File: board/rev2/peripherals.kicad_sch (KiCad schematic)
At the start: 8 parts, among them J3 USB_C_Receptacle_USB2.0_14P, J6 Micro_SD_Card_Det1, J7 Conn_01x09_Pin, SW1 SW_Push

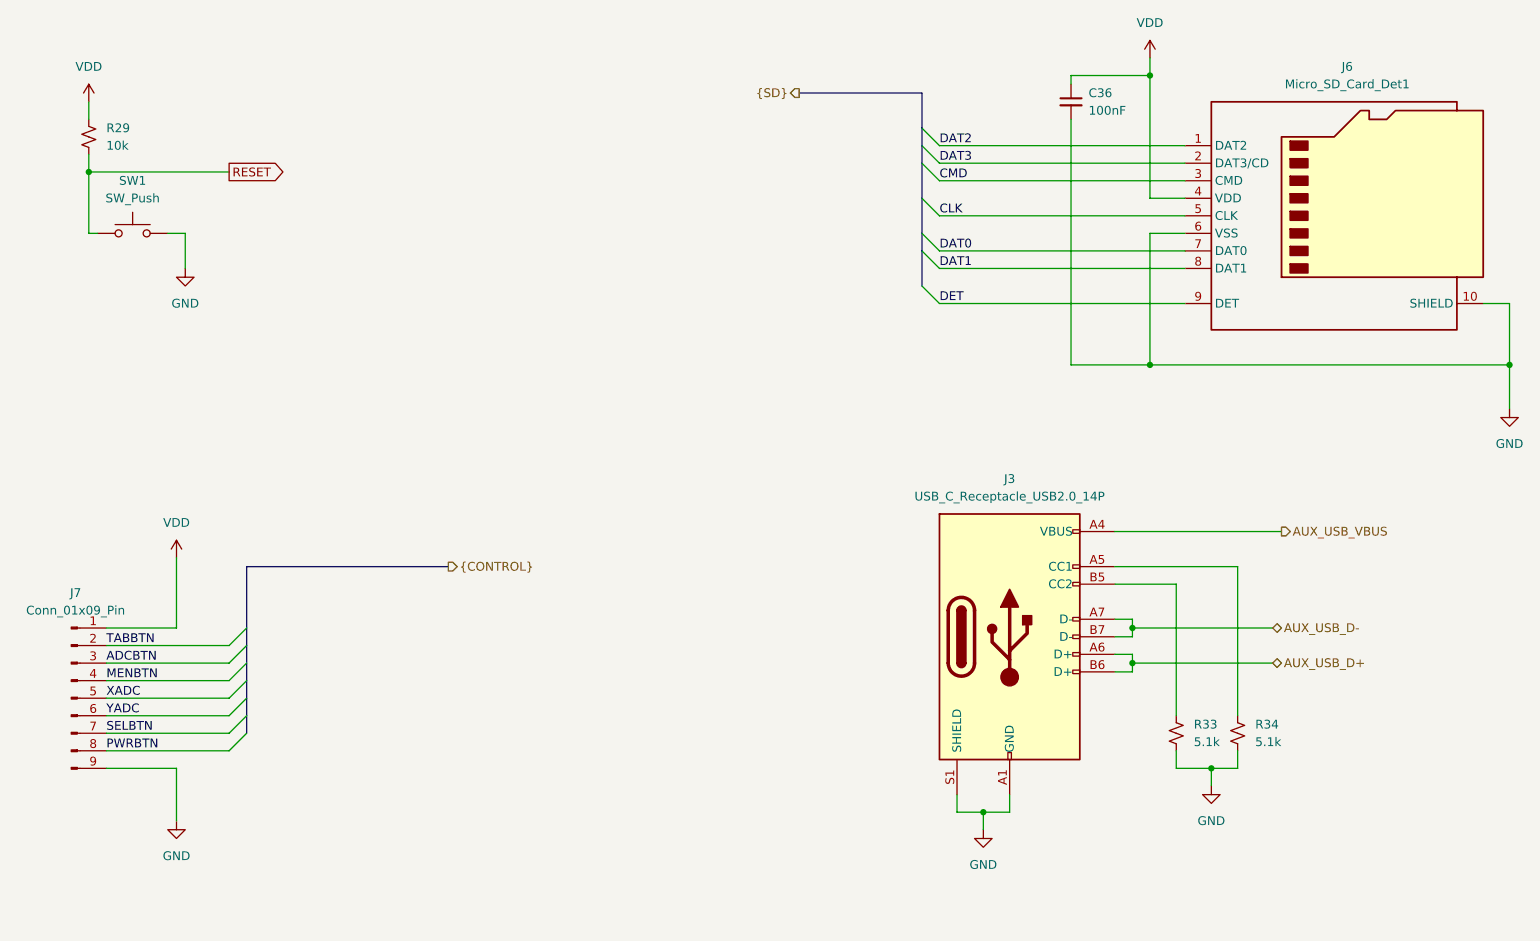
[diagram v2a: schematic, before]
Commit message: Start new PCB
- all footprints setup
- need to setup netclasses next, tho
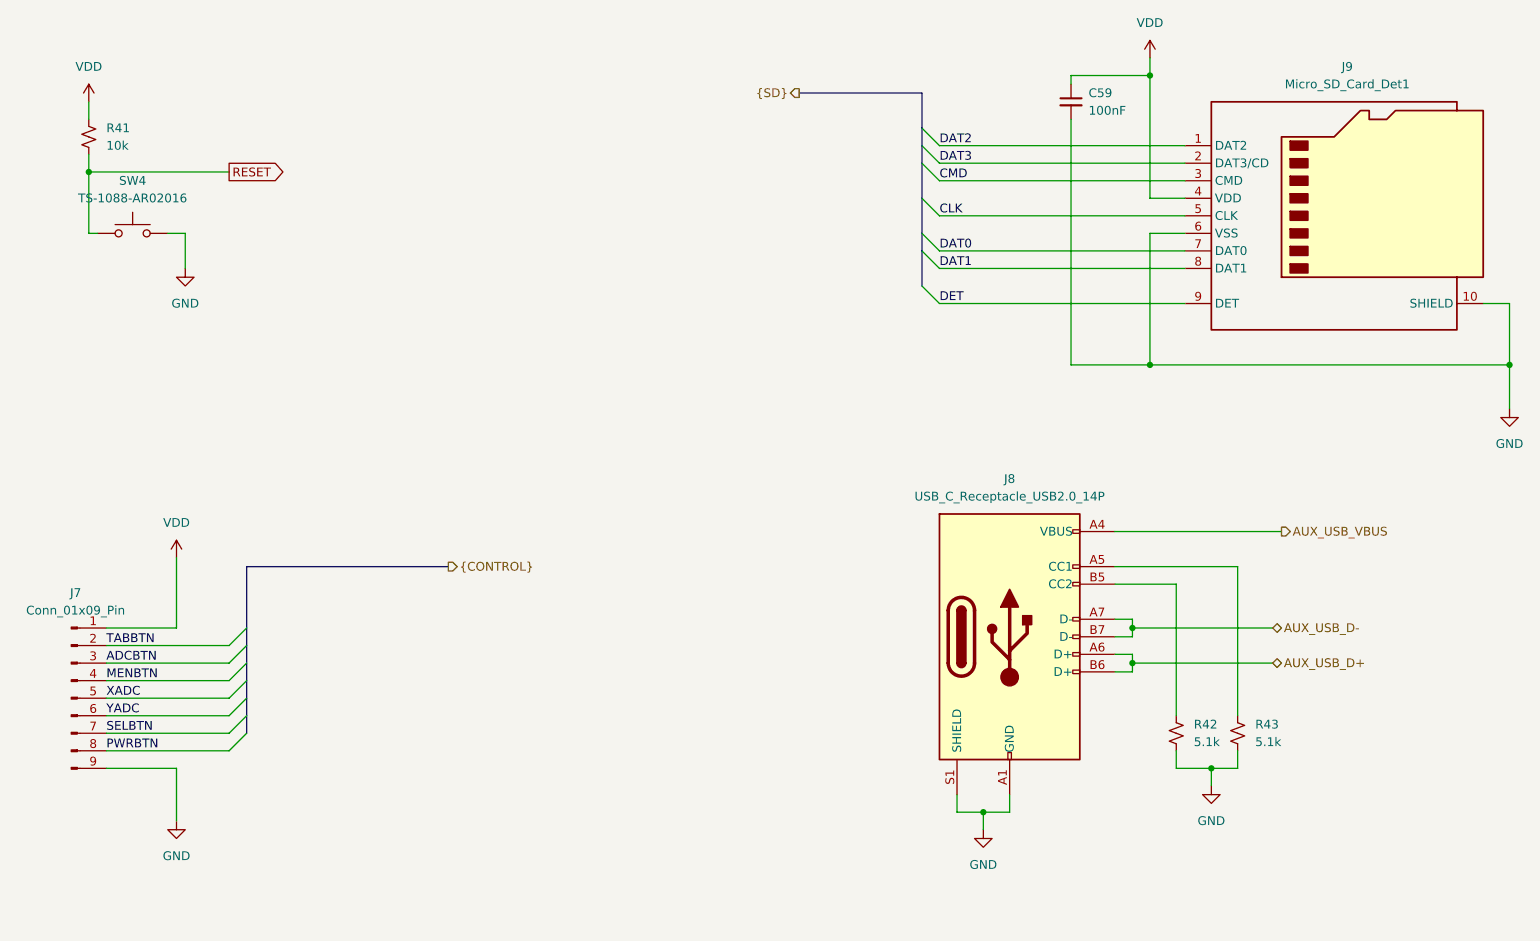
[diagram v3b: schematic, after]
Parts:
- J8: renamed from J3; footprint (none) -> Connector_USB:USB_C_Receptacle_HRO_TYPE-C-31-M-12; Part (none) -> TYPE-C-31-M-12
- J9: renamed from J6; Part (none) -> DM3AT-SF-PEJM5
- SW4: renamed from SW1; value SW_Push -> TS-1088-AR02016; footprint (none) -> Button_Switch_SMD:SW_SPST_TS-1088-xR020; Part (none) -> TS-1088-AR02016
- renumbered C36 to C59, R29 to R41, R33 to R42, R34 to R43
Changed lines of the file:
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@@
 		(dnp no)
 		(fields_autoplaced yes)
-		(property "Reference" "SW1"
+		(property "Reference" "SW4"
 			(at 57.15 54.61 0)
 			(effects
@@
 			)
 		)
-		(property "Value" "SW_Push"
+		(property "Value" "TS-1088-AR02016"
 			(at 57.15 57.15 0)
 			(effects
@@
 			)
 		)
-		(property "Footprint" ""
+		(property "Footprint" "Button_Switch_SMD:SW_SPST_TS-1088-xR020"
 			(at 57.15 57.15 0)
 			(effects
@@
 			)
 		)
+		(property "Part" "TS-1088-AR02016"
+			(at 57.15 62.23 0)
+			(effects
+				(font
+					(size 1.27 1.27)
+				)
+				(hide yes)
+			)
+		)
 		(pin "1"
 		)
@@
 			(project ""
 				(path "/32eb05c7-b4a6-42f3-8fb3-43453631100f/802ce1c9-2668-4fe7-971c-9ba57eb1ffa9"
-					(reference "SW1")
+					(reference "SW4")
 					(unit 1)
 				)
@@
 		(dnp no)
 		(fields_autoplaced yes)
-		(property "Reference" "#PWR038"
+		(property "Reference" "#PWR054"
 			(at 204.47 40.64 0)
 			(effects
@@
 			(project ""
 				(path "/32eb05c7-b4a6-42f3-8fb3-43453631100f/802ce1c9-2668-4fe7-971c-9ba57eb1ffa9"
-					(reference "#PWR038")
+					(reference "#PWR054")
 					(unit 1)
 				)
@@
 		(dnp no)
 		(fields_autoplaced yes)
-		(property "Reference" "J6"
+		(property "Reference" "J9"
 			(at 233.045 38.1 0)
 			(effects
@@
 			)
 		)
+		(property "Part" "DM3AT-SF-PEJM5"
+			(at 232.41 59.69 0)
+			(effects
+				(font
+					(size 1.27 1.27)
+				)
+				(hide yes)
+			)
+		)
 		(pin "1"
 		)
@@
 			(project ""
 				(path "/32eb05c7-b4a6-42f3-8fb3-43453631100f/802ce1c9-2668-4fe7-971c-9ba57eb1ffa9"
-					(reference "J6")
+					(reference "J9")
 					(unit 1)
 				)
@@
 		(dnp no)
 		(fields_autoplaced yes)
-		(property "Reference" "#PWR014"
+		(property "Reference" "#PWR055"
 			(at 213.36 148.59 0)
 			(effects
@@
 			(project ""
 				(path "/32eb05c7-b4a6-42f3-8fb3-43453631100f/802ce1c9-2668-4fe7-971c-9ba57eb1ffa9"
-					(reference "#PWR014")
+					(reference "#PWR055")
 					(unit 1)
 				)
@@
 		(dnp no)
 		(fields_autoplaced yes)
-		(property "Reference" "J3"
+		(property "Reference" "J8"
 			(at 184.15 97.79 0)
 			(effects
@@
 			)
 		)
-		(property "Footprint" ""
+		(property "Footprint" "Connector_USB:USB_C_Receptacle_HRO_TYPE-C-31-M-12"
 			(at 187.96 120.65 0)
 			(effects
@@
 			)
 		)
+		(property "Part" "TYPE-C-31-M-12"
+			(at 184.15 120.65 0)
+			(effects
+				(font
+					(size 1.27 1.27)
+				)
+				(hide yes)
+			)
+		)
 		(pin "B6"
 		)
@@
 			(project "mainboard"
 				(path "/32eb05c7-b4a6-42f3-8fb3-43453631100f/802ce1c9-2668-4fe7-971c-9ba57eb1ffa9"
-					(reference "J3")
+					(reference "J8")
 					(unit 1)
 				)
@@
 		(dnp no)
 		(fields_autoplaced yes)
-		(property "Reference" "#PWR013"
+		(property "Reference" "#PWR053"
 			(at 180.34 154.94 0)
 			(effects
@@
 			(project "mainboard"
 				(path "/32eb05c7-b4a6-42f3-8fb3-43453631100f/802ce1c9-2668-4fe7-971c-9ba57eb1ffa9"
-					(reference "#PWR013")
+					(reference "#PWR053")
 					(unit 1)
 				)
@@
 		(dnp no)
 		(fields_autoplaced yes)
-		(property "Reference" "#PWR02"
+		(property "Reference" "#PWR049"
 			(at 50.8 46.99 0)
 			(effects
@@
 			(project "mainboard"
 				(path "/32eb05c7-b4a6-42f3-8fb3-43453631100f/802ce1c9-2668-4fe7-971c-9ba57eb1ffa9"
-					(reference "#PWR02")
+					(reference "#PWR049")
 					(unit 1)
 				)
@@
 		(dnp no)
 		(fields_autoplaced yes)
-		(property "Reference" "R34"
+		(property "Reference" "R43"
 			(at 219.71 133.3499 0)
 			(effects
@@
 			(project ""
 				(path "/32eb05c7-b4a6-42f3-8fb3-43453631100f/802ce1c9-2668-4fe7-971c-9ba57eb1ffa9"
-					(reference "R34")
+					(reference "R43")
 					(unit 1)
 				)
@@
 		(dnp no)
 		(fields_autoplaced yes)
-		(property "Reference" "C36"
+		(property "Reference" "C59"
 			(at 195.58 41.9162 0)
 			(effects
@@
 			(project ""
 				(path "/32eb05c7-b4a6-42f3-8fb3-43453631100f/802ce1c9-2668-4fe7-971c-9ba57eb1ffa9"
-					(reference "C36")
+					(reference "C59")
 					(unit 1)
 				)
@@
 		(dnp no)
 		(fields_autoplaced yes)
-		(property "Reference" "#PWR039"
+		(property "Reference" "#PWR050"
 			(at 63.5 113.03 0)
 			(effects
@@
 			(project ""
 				(path "/32eb05c7-b4a6-42f3-8fb3-43453631100f/802ce1c9-2668-4fe7-971c-9ba57eb1ffa9"
-					(reference "#PWR039")
+					(reference "#PWR050")
 					(unit 1)
 				)
@@
 		(dnp no)
 		(fields_autoplaced yes)
-		(property "Reference" "#PWR028"
+		(property "Reference" "#PWR052"
 			(at 64.77 73.66 0)
 			(effects
@@
 			(project ""
 				(path "/32eb05c7-b4a6-42f3-8fb3-43453631100f/802ce1c9-2668-4fe7-971c-9ba57eb1ffa9"
-					(reference "#PWR028")
+					(reference "#PWR052")
 					(unit 1)
 				)
@@
 		(dnp no)
 		(fields_autoplaced yes)
-		(property "Reference" "R29"
+		(property "Reference" "R41"
 			(at 53.34 46.9899 0)
 			(effects
@@
 			(project ""
 				(path "/32eb05c7-b4a6-42f3-8fb3-43453631100f/802ce1c9-2668-4fe7-971c-9ba57eb1ffa9"
-					(reference "R29")
+					(reference "R41")
 					(unit 1)
 				)
@@
 		(dnp no)
 		(fields_autoplaced yes)
-		(property "Reference" "#PWR029"
+		(property "Reference" "#PWR056"
 			(at 256.54 93.98 0)
 			(effects
@@
 			(project ""
 				(path "/32eb05c7-b4a6-42f3-8fb3-43453631100f/802ce1c9-2668-4fe7-971c-9ba57eb1ffa9"
-					(reference "#PWR029")
+					(reference "#PWR056")
 					(unit 1)
 				)
@@
 		(dnp no)
 		(fields_autoplaced yes)
-		(property "Reference" "R33"
+		(property "Reference" "R42"
 			(at 210.82 133.3499 0)
 			(effects
@@
 			(project ""
 				(path "/32eb05c7-b4a6-42f3-8fb3-43453631100f/802ce1c9-2668-4fe7-971c-9ba57eb1ffa9"
-					(reference "R33")
+					(reference "R42")
 					(unit 1)
 				)
@@
 		(dnp no)
 		(fields_autoplaced yes)
-		(property "Reference" "#PWR040"
+		(property "Reference" "#PWR051"
 			(at 63.5 153.67 0)
 			(effects
@@
 			(project ""
 				(path "/32eb05c7-b4a6-42f3-8fb3-43453631100f/802ce1c9-2668-4fe7-971c-9ba57eb1ffa9"
-					(reference "#PWR040")
-					(unit 1)
-				)
+					(reference "#PWR051")
+					(unit 1)
+				)

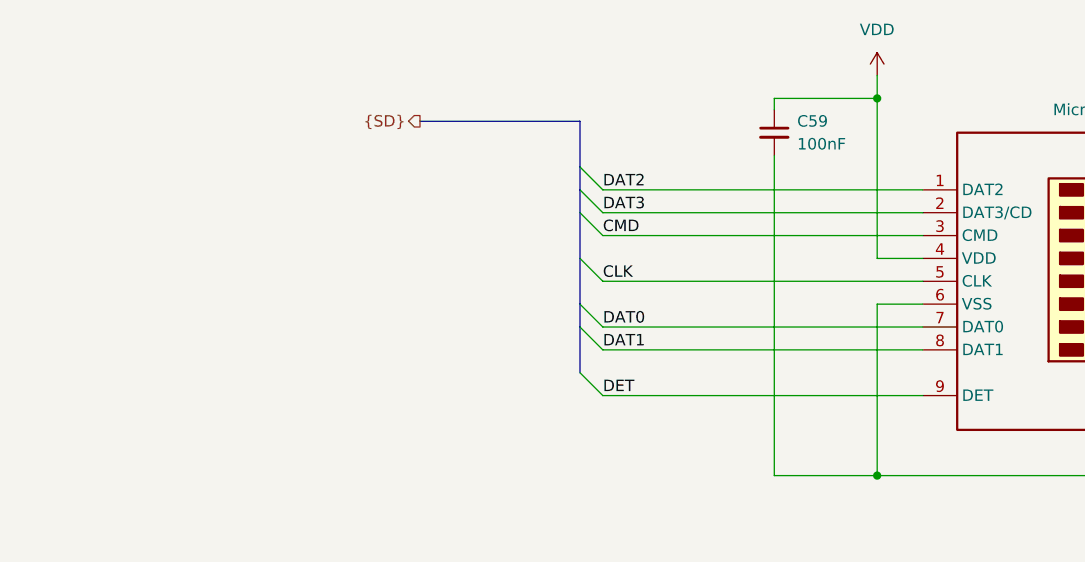
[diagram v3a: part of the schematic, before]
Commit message: Add netclasses, more footprints, fix ERC
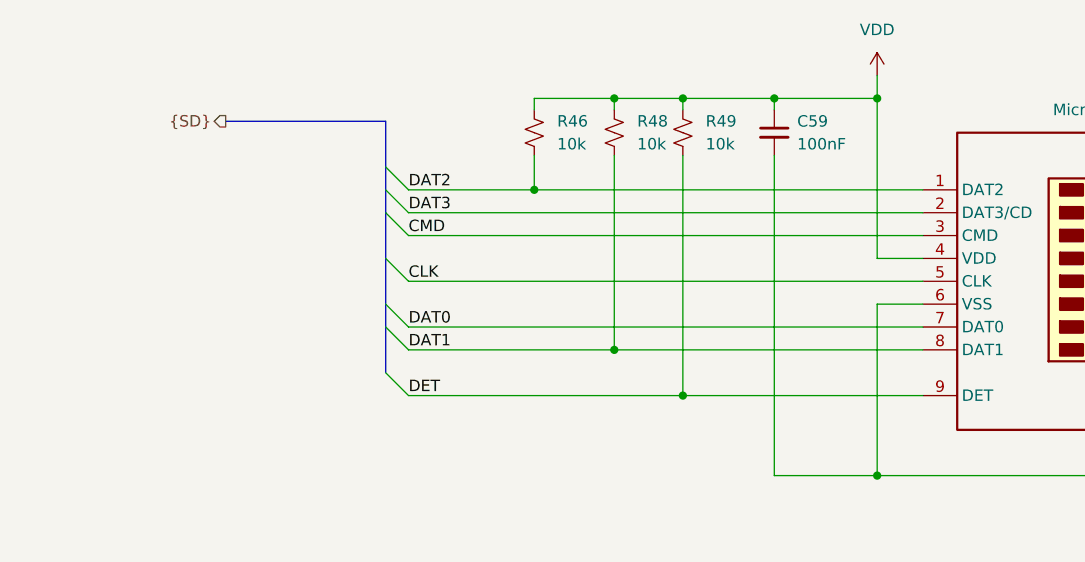
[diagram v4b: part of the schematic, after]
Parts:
- added R46, R48, R49: 10k, symbol Device:R_Small_US
- J9: footprint Connector_Card:microSD_HC_Hirose_DM3AT-SF-PEJM5 -> Connector_TF:microSD_XUNPU_TF-115-BCP9; Part DM3AT-SF-PEJM5 -> TF-115-BCP9
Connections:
- net DAT1: now also R48.2
- net DAT2: now also R46.2
- net DET: now also R49.2
- net VDD: now also R46.1, R48.1, R49.1
